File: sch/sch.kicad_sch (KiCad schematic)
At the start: 53 parts, among them U1 Pico, U2 PCA9548ADB, U3 MPR121QR2_BOARD, U4 MPR121QR2_BOARD, U5 MPR121QR2_BOARD

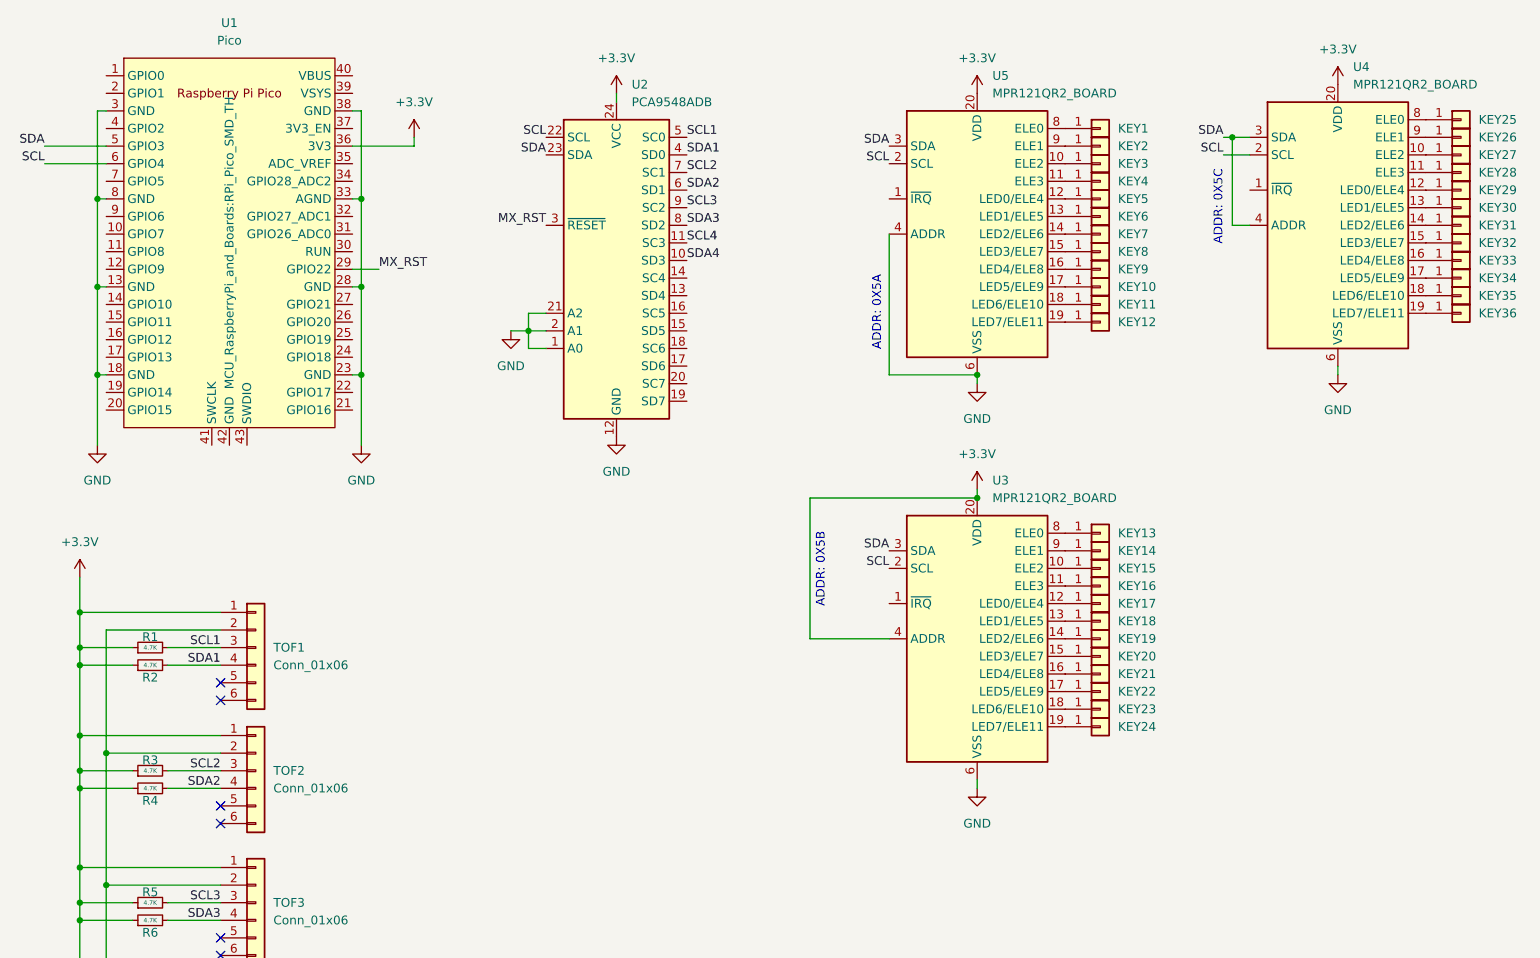
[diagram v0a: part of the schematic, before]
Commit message: Updated schematic for Pro Micro
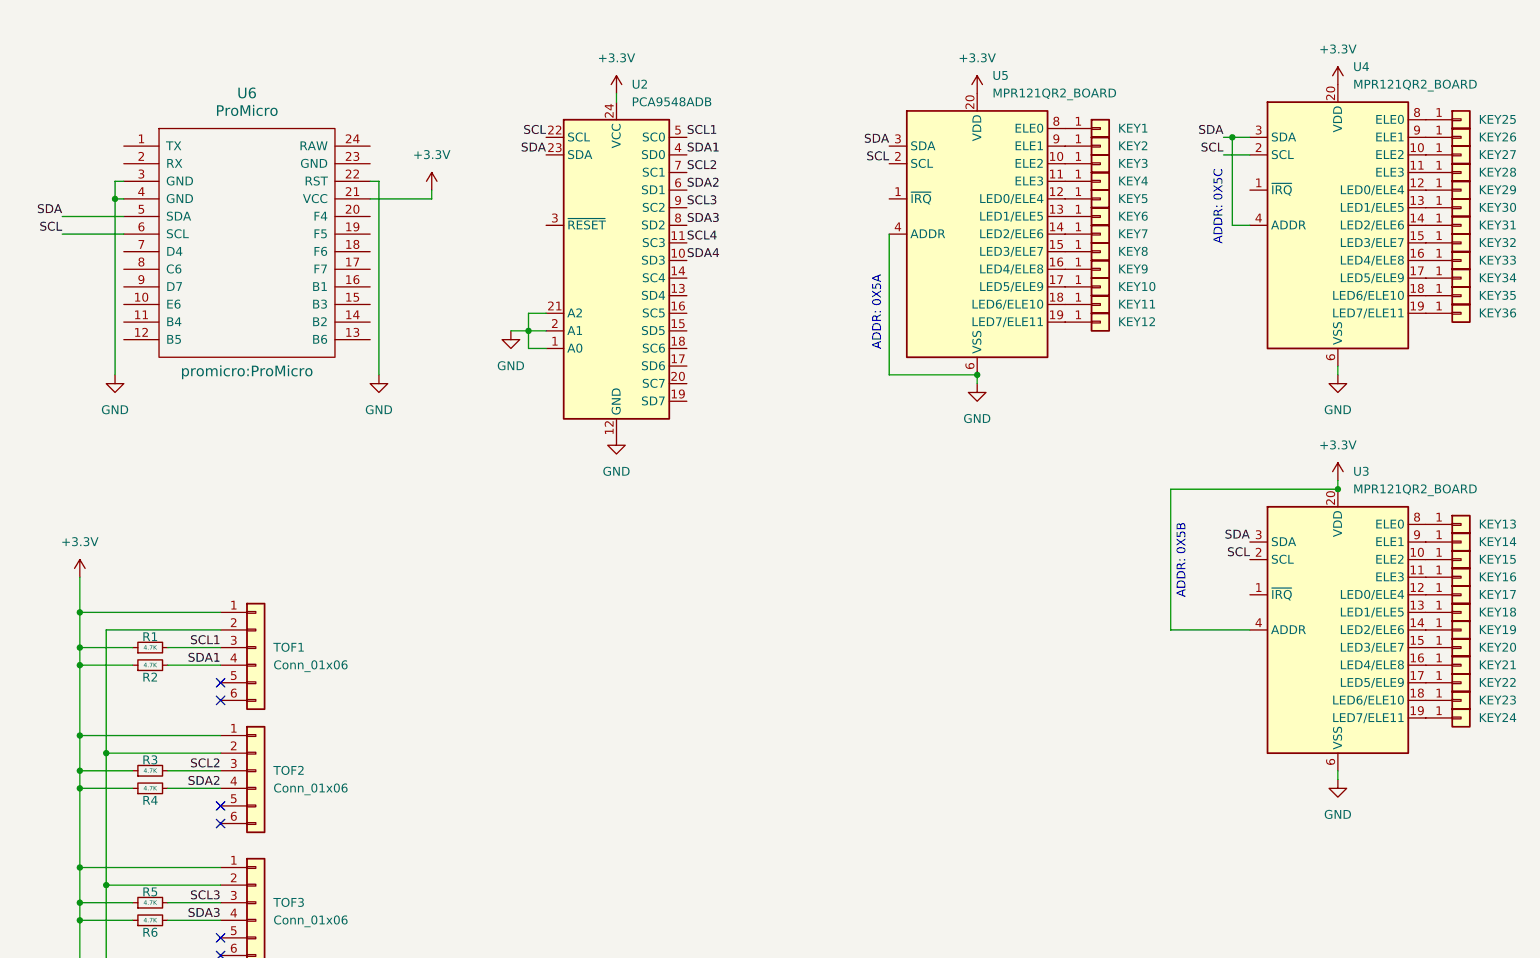
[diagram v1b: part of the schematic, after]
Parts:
- removed U1: Pico, MCU_RaspberryPi_and_Boards:RPi_Pico_SMD_TH, symbol MCU_RaspberryPi_and_Boards:Pico
- added U6: ProMicro, promicro:ProMicro, symbol promicro:ProMicro
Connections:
- net +3.3V: now also U6.21 (VCC)
- net GND: now also U6.22 (RST), U6.3 (GND), U6.4 (GND)
- net SCL: now also U6.6 (SCL)
- net SDA: now also U6.5 (SDA)
- net MX_RST: no longer names the net of U2.3 (~{RESET})
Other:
- moved on the sheet: KEY13, KEY14, KEY15, KEY16, KEY17, KEY18, KEY19, KEY20, KEY21, KEY22, KEY23, KEY24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

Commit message: fixed missing pull up on multiplexer
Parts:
- added R9: 4.7K, Resistor_SMD:R_0603_1608Metric, symbol Device:R_Small
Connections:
- net +3.3V: now also R9.1
- net at U2.3 (~{RESET}): now also R9.2
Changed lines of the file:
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@@
 (kicad_sch
-	(version 20231120)
+	(version 20250114)
 	(generator "eeschema")
-	(generator_version "8.0")
+	(generator_version "9.0")
 	(paper "A4")
+	(text "ADDR: 0X5C"
+		(exclude_from_sim no)
+		(at 193.548 45.72 90)
+		(effects
+			(font
+				(size 1.27 1.27)
+			)
+		)
+	)
+	(text "ADDR: 0X5A"
+		(exclude_from_sim no)
+		(at 144.272 60.96 90)
+		(effects
+			(font
+				(size 1.27 1.27)
+			)
+		)
+	)
+	(text "ADDR: 0X5B"
+		(exclude_from_sim no)
+		(at 188.214 96.774 90)
+		(effects
+			(font
+				(size 1.27 1.27)
+			)
+		)
+	)
 	(junction
 		(at 34.29 44.45)
@@
 	(wire
 		(pts
+			(xy 91.44 48.26) (xy 90.17 48.26)
+		)
+		(stroke
+			(width 0)
+			(type default)
+		)
+	)
+	(wire
+		(pts
 			(xy 29.21 104.14) (xy 29.21 109.22)
 		)
@@
 	(wire
 		(pts
+			(xy 90.17 46.99) (xy 90.17 48.26)
+		)
+		(stroke
+			(width 0)
+			(type default)
+		)
+	)
+	(wire
+		(pts
 			(xy 33.02 124.46) (xy 49.53 124.46)
 		)
@@
 		)
 	)
-	(text "ADDR: 0X5C"
-		(exclude_from_sim no)
-		(at 193.548 45.72 90)
-		(effects
-			(font
-				(size 1.27 1.27)
-			)
-		)
-	)
-	(text "ADDR: 0X5A"
-		(exclude_from_sim no)
-		(at 144.272 60.96 90)
-		(effects
-			(font
-				(size 1.27 1.27)
-			)
-		)
-	)
-	(text "ADDR: 0X5B"
-		(exclude_from_sim no)
-		(at 188.214 96.774 90)
-		(effects
-			(font
-				(size 1.27 1.27)
-			)
-		)
-	)
 	(label "SCL3"
 		(at 49.53 146.05 180)
-		(fields_autoplaced yes)
 		(effects
 			(font
@@
 	(label "SCL"
 		(at 26.67 49.53 180)
-		(fields_autoplaced yes)
 		(effects
 			(font
@@
 	(label "SCL4"
 		(at 116.84 50.8 0)
-		(fields_autoplaced yes)
 		(effects
 			(font
@@
 	(label "SCL"
 		(at 198.12 96.52 180)
-		(fields_autoplaced yes)
 		(effects
 			(font
@@
 	(label "SDA2"
 		(at 49.53 129.54 180)
-		(fields_autoplaced yes)
 		(effects
 			(font
@@
 	(label "SDA1"
 		(at 49.53 111.76 180)
-		(fields_autoplaced yes)
 		(effects
 			(font
@@
 	(label "SDA"
 		(at 194.31 35.56 180)
-		(fields_autoplaced yes)
 		(effects
 			(font
@@
 	(label "SCL1"
 		(at 49.53 109.22 180)
-		(fields_autoplaced yes)
 		(effects
 			(font
@@
 	(label "SDA"
 		(at 198.12 93.98 180)
-		(fields_autoplaced yes)
 		(effects
 			(font
@@
 	(label "SDA"
 		(at 26.67 46.99 180)
-		(fields_autoplaced yes)
 		(effects
 			(font
@@
 	(label "SCL1"
 		(at 116.84 35.56 0)
-		(fields_autoplaced yes)
 		(effects
 			(font
@@
 	(label "SDA1"
 		(at 116.84 38.1 0)
-		(fields_autoplaced yes)
 		(effects
 			(font
@@
 	(label "SCL"
 		(at 96.52 35.56 180)
-		(fields_autoplaced yes)
 		(effects
 			(font
@@
 	(label "SCL3"
 		(at 116.84 45.72 0)
-		(fields_autoplaced yes)
 		(effects
 			(font
@@
 	(label "SCL2"
 		(at 116.84 40.64 0)
-		(fields_autoplaced yes)
 		(effects
 			(font
@@
 	(label "SDA4"
 		(at 116.84 53.34 0)
-		(fields_autoplaced yes)
 		(effects
 			(font
@@
 	(label "SDA3"
 		(at 49.53 148.59 180)
-		(fields_autoplaced yes)
 		(effects
 			(font
@@
 	(label "SDA3"
 		(at 116.84 48.26 0)
-		(fields_autoplaced yes)
 		(effects
 			(font
@@
 	(label "SDA4"
 		(at 49.53 166.37 180)
-		(fields_autoplaced yes)
 		(effects
 			(font
@@
 	(label "SCL"
 		(at 146.05 39.37 180)
-		(fields_autoplaced yes)
 		(effects
 			(font
@@
 	(label "SDA"
 		(at 96.52 38.1 180)
-		(fields_autoplaced yes)
 		(effects
 			(font
@@
 	(label "SDA"
 		(at 146.05 36.83 180)
-		(fields_autoplaced yes)
 		(effects
 			(font
@@
 	(label "SCL2"
 		(at 49.53 127 180)
-		(fields_autoplaced yes)
 		(effects
 			(font
@@
 	(label "SCL4"
 		(at 49.53 163.83 180)
-		(fields_autoplaced yes)
 		(effects
 			(font
@@
 	(label "SDA2"
 		(at 116.84 43.18 0)
-		(fields_autoplaced yes)
 		(effects
 			(font
@@
 	(label "SCL"
 		(at 194.31 38.1 180)
-		(fields_autoplaced yes)
 		(effects
 			(font
@@
 	)
 	(symbol
+		(lib_id "power:+3.3V")
+		(at 90.17 46.99 0)
+		(unit 1)
+		(exclude_from_sim no)
+		(in_bom yes)
+		(on_board yes)
+		(dnp no)
+		(fields_autoplaced yes)
+		(property "Reference" "#PWR05"
+			(at 90.17 50.8 0)
+			(effects
+				(font
+					(size 1.27 1.27)
+				)
+				(hide yes)
+			)
+		)
+		(property "Value" "+3.3V"
+			(at 90.17 41.91 0)
+			(effects
+				(font
+					(size 1.27 1.27)
+				)
+			)
+		)
+		(property "Footprint" ""
+			(at 90.17 46.99 0)
+			(effects
+				(font
+					(size 1.27 1.27)
+				)
+				(hide yes)
+			)
+		)
+		(property "Datasheet" ""
+			(at 90.17 46.99 0)
+			(effects
+				(font
+					(size 1.27 1.27)
+				)
+				(hide yes)
+			)
+		)
+		(property "Description" "Power symbol creates a global label with name \"+3.3V\""
+			(at 90.17 46.99 0)
+			(effects
+				(font
+					(size 1.27 1.27)
+				)
+				(hide yes)
+			)
+		)
+		(pin "1"
+		)
+		(instances
+			(project "sch"
+				(path "/1dc86d34-d36d-4f25-9b18-9efd82e840fc"
+					(reference "#PWR05")
+					(unit 1)
+				)
+			)
+		)
+	)
+	(symbol
 		(lib_id "Device:R_Small")
 		(at 39.37 148.59 90)
@@
 	)
 	(symbol
+		(lib_id "Device:R_Small")
+		(at 93.98 48.26 90)
+		(unit 1)
+		(exclude_from_sim no)
+		(in_bom yes)
+		(on_board yes)
+		(dnp no)
+		(property "Reference" "R9"
+			(at 93.98 46.736 90)
+			(effects
+				(font
+					(size 1.27 1.27)
+				)
+			)
+		)
+		(property "Value" "4.7K"
+			(at 93.98 48.26 90)
+			(effects
+				(font
+					(size 0.635 0.635)
+				)
+			)
+		)
+		(property "Footprint" "Resistor_SMD:R_0603_1608Metric"
+			(at 93.98 48.26 0)
+			(effects
+				(font
+					(size 1.27 1.27)
+				)
+				(hide yes)
+			)
+		)
+		(property "Datasheet" "~"
+			(at 93.98 48.26 0)
+			(effects
+				(font
+					(size 1.27 1.27)
+				)
+				(hide yes)
+			)
+		)
+		(property "Description" "Resistor, small symbol"
+			(at 93.98 48.26 0)
+			(effects
+				(font
+					(size 1.27 1.27)
+				)
+				(hide yes)
+			)
+		)
+		(pin "1"
+		)
+		(pin "2"
+		)
+		(instances
+			(project "sch"
+				(path "/1dc86d34-d36d-4f25-9b18-9efd82e840fc"
+					(reference "R9")
+					(unit 1)
+				)
+			)
+		)
+	)
+	(symbol
 		(lib_id "power:GND")
 		(at 210.82 128.27 0)
@@
 		)
 	)
+	(embedded_fonts no)
 )
